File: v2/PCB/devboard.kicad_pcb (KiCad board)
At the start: 2 copper layers, 51 x 21 mm, 4 parts, among them J1 USB_C_Receptacle_USB2.0_14P, J2 Conn_01x20, J3 Conn_01x20, J4 Conn_01x03

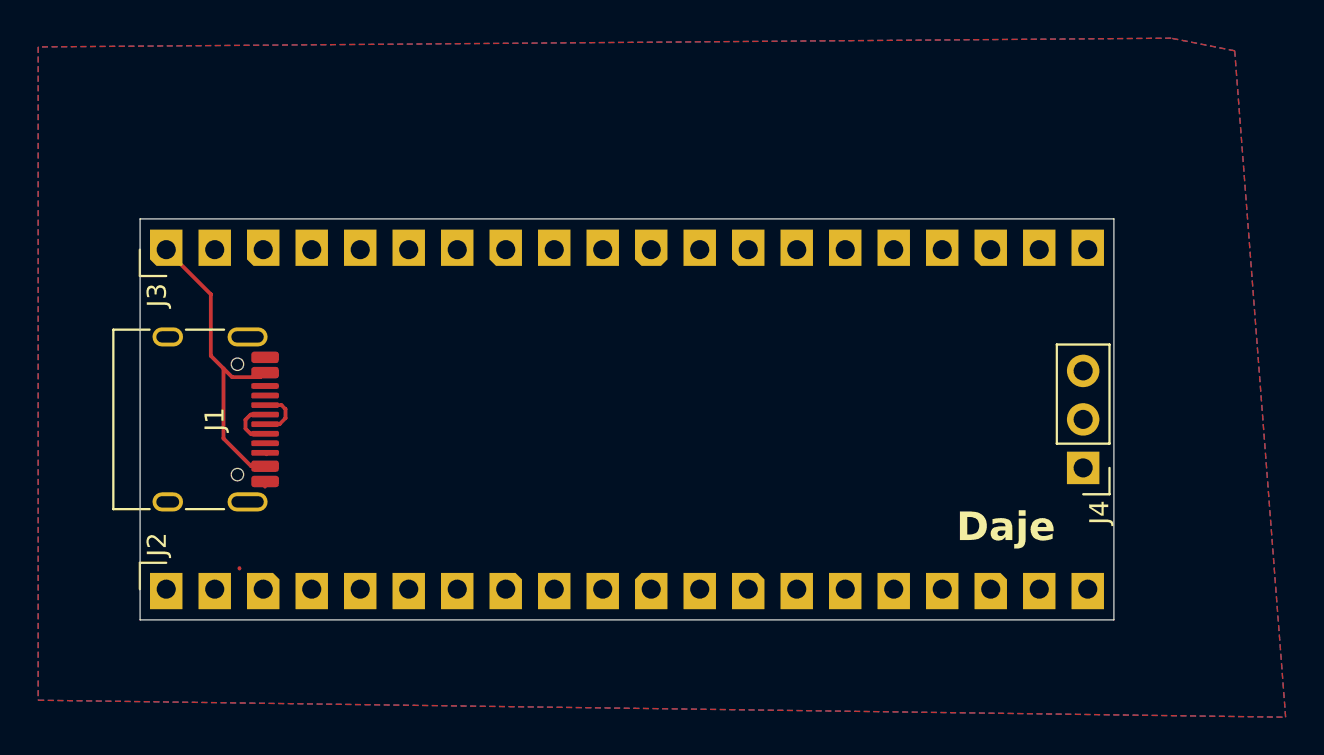
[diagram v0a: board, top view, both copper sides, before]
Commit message: added imu to the v2 and created/wired pcb
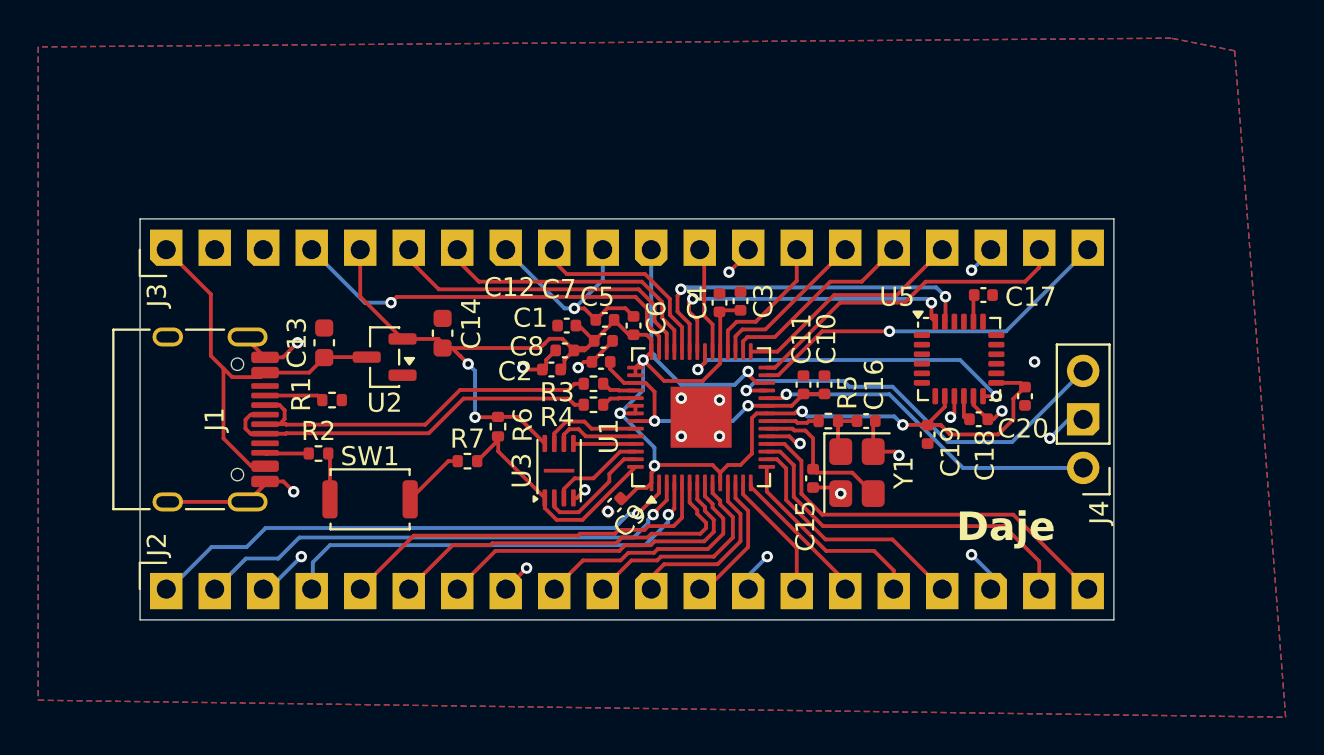
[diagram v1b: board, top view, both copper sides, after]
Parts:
- added C1: 1uF, Capacitor_SMD:C_0402_1005Metric, F.Cu at (111.5, 62.6)
- added C10: 0.1uF, Capacitor_SMD:C_0402_1005Metric, F.Cu at (125.0, 65.7)
- added C11: 0.1uF, Capacitor_SMD:C_0402_1005Metric, F.Cu at (123.9, 65.7)
- added C12: 1uF, Capacitor_SMD:C_0402_1005Metric, F.Cu at (113.3, 64.5)
- added C13: 10uF, Capacitor_SMD:C_0603_1608Metric, F.Cu at (98.8, 63.5)
- added C14: 10uF, Capacitor_SMD:C_0603_1608Metric, F.Cu at (105.0, 63.0)
- added C15: 33pF, Capacitor_SMD:C_0402_1005Metric, F.Cu at (124.4, 70.6)
- added C16: 33pF, Capacitor_SMD:C_0402_1005Metric, F.Cu at (127.2, 67.6)
- added C17: 2.2Nf, Capacitor_SMD:C_0402_1005Metric, F.Cu at (133.3, 61.0)
- added C18: 0.1uF, Capacitor_SMD:C_0402_1005Metric, F.Cu at (133.1, 67.5)
- added C19: 10nF, Capacitor_SMD:C_0402_1005Metric, F.Cu at (130.4, 68.3)
- added C2: 0.1uF, Capacitor_SMD:C_0402_1005Metric, F.Cu at (110.7, 64.9)
- added C20: 0.1uF, Capacitor_SMD:C_0402_1005Metric, F.Cu at (135.5, 66.3)
- added C3: 0.1uF, Capacitor_SMD:C_0402_1005Metric, F.Cu at (120.6, 61.3)
- added C4: 0.1uF, Capacitor_SMD:C_0402_1005Metric, F.Cu at (119.5, 61.4)
- added C5: 0.1uF, Capacitor_SMD:C_0402_1005Metric, F.Cu at (113.5, 62.3)
- added C6: 0.1uF, Capacitor_SMD:C_0402_1005Metric, F.Cu at (115.0, 62.6)
- added C7: 0.1uF, Capacitor_SMD:C_0402_1005Metric, F.Cu at (113.4, 63.4)
- added C8: 0.1uF, Capacitor_SMD:C_0402_1005Metric, F.Cu at (111.4, 63.9)
- added C9: 0.1uF, Capacitor_SMD:C_0402_1005Metric, F.Cu at (114.0, 72.0)
- added R1: 5.1K, Resistor_SMD:R_0402_1005Metric, F.Cu at (99.2, 66.5)
- added R2: 5.1K, Resistor_SMD:R_0402_1005Metric, F.Cu at (98.5, 69.3)
- added R3: 27, Resistor_SMD:R_0402_1005Metric, F.Cu at (112.9, 65.6)
- added R4: 27, Resistor_SMD:R_0402_1005Metric, F.Cu at (112.9, 66.7)
- added R5: 1K, Resistor_SMD:R_0402_1005Metric, F.Cu at (125.2, 67.6)
- added R6: 10K, Resistor_SMD:R_0402_1005Metric, F.Cu at (107.9, 67.9)
- added R7: 1K, Resistor_SMD:R_0402_1005Metric, F.Cu at (106.3, 69.7)
- added SW1: SW_Push, Button_Switch_SMD:SW_Push_SPST_NO_Alps_SKRK, F.Cu at (101.2, 71.7)
- added U1: RP2040, Package_DFN_QFN:QFN-56-1EP_7x7mm_P0.4mm_EP3.2x3.2mm, F.Cu at (118.5, 67.4)
- added U2: MCP1700x-330xxTT, Package_TO_SOT_SMD:SOT-23, F.Cu at (102.0, 64.2)
- added U3: W25Q16JVUXIQ TR, Package_SON:Winbond_USON-8-1EP_3x2mm_P0.5mm_EP0.2x1.6mm, F.Cu at (111.1, 70.2)
- added U5: MPU-6050, Sensor_Motion:InvenSense_QFN-24_4x4mm_P0.5mm, F.Cu at (132.1, 64.3)
- added Y1: Crystal_GND24, Crystal:Crystal_SMD_3225-4Pin_3.2x2.5mm, F.Cu at (126.7, 70.3)
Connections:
- J3 pad 10: GPIO23 -> GND
- J3 pad 2: GPIO29_ADC3 -> GND
- J3 pad 4: GPIO28_ADC2 -> GPIO29_ADC3
- J3 pad 6: GPIO27_ADC1 -> GPIO28_ADC2
- J3 pad 7: GPIO26_ADC0 -> GPIO27_ADC1
- J3 pad 9: GPIO24 -> GPIO26_ADC0
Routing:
- net +3.3V: track 0.00 -> 83.9 mm, vias 0 -> 7
- net GND: track 1.28 -> 56.4 mm, vias 0 -> 24
- net GPIO0: track 0.00 -> 28.4 mm, vias 0 -> 1
- net GPIO1: track 0.00 -> 28.1 mm, vias 0 -> 1
- net GPIO2: track 0.00 -> 23.1 mm, vias 0 -> 1
- net SWD: track 0.00 -> 21.8 mm, vias 0 -> 1
- net GPIO29_ADC3: track 0.00 -> 21.6 mm, vias 0 -> 1
- net GPIO15: track 0.00 -> 21.0 mm
- net GPIO3: track 0.00 -> 20.2 mm
- net GPIO4: track 0.00 -> 19.6 mm
- net GPIO16: track 0.00 -> 19.5 mm, vias 0 -> 1
- net GPIO14: track 0.00 -> 19.1 mm
- net SCL: track 0.00 -> 19.0 mm, vias 0 -> 2
- net SWCLK: track 0.00 -> 18.2 mm, vias 0 -> 1
- net GPIO23: track 0.36 -> 18.5 mm, vias 0 -> 2
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
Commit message: updated pcb and made renders
-Changed imu to a MPU-6500
-moved some traces and changed some pads in the devboard
-remade gerber and BOM
-created renders of the v2
-made pinout image of the v2
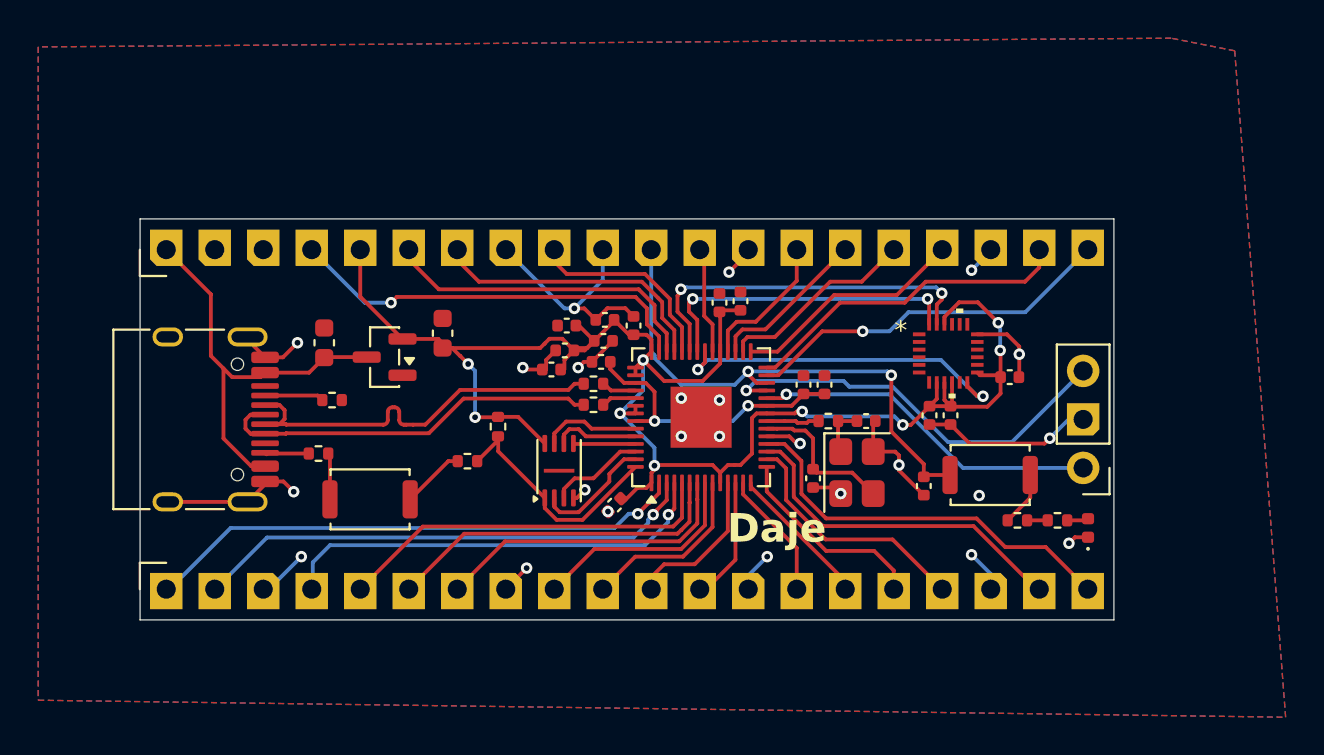
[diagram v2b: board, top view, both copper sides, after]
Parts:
- removed C17: 2.2Nf, Capacitor_SMD:C_0402_1005Metric
- removed C19: 10nF, Capacitor_SMD:C_0402_1005Metric
- added C21: 100nF, Capacitor_SMD:C_0402_1005Metric, F.Cu at (130.2, 71.0)
- added C22: 10nF, Capacitor_SMD:C_0402_1005Metric, F.Cu at (130.5, 67.3)
- added D2: LED, LED_SMD:LED_0402_1005Metric, F.Cu at (138.8, 73.2)
- added R8: 1K, Resistor_SMD:R_0402_1005Metric, F.Cu at (135.1, 72.8)
- added R9: 150, Resistor_SMD:R_0402_1005Metric, F.Cu at (137.2, 72.8)
- added SW2: SW_Push, Button_Switch_SMD:SW_Push_SPST_NO_Alps_SKRK, F.Cu at (133.7, 70.4)
- U5: value MPU-6050 -> MPU-6500; footprint Sensor_Motion:InvenSense_QFN-24_4x4mm_P0.5mm -> mpu 6500:QFN24_3X3X0P9_IVS
- moved C20 4.03 mm to (131.6, 67.3), turned to -90 degrees
- moved C18 2.74 mm to (134.7, 65.3)
- moved U5 0.64 mm to (131.5, 64.1)
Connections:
- C18 pad 1: Net-(U5-REGOUT) -> +3.3V
- C20 pad 1: GND -> +3.3V
- C20 pad 2: +3.3V -> GND
- U5 pad 1: GND -> unconnected-(U5-NC-Pad1)
- U5 pad 10: Net-(U5-REGOUT) -> +3.3V
- U5 pad 11: GND -> unconnected-(U5-FSYNC-Pad11)
- U5 pad 20: Net-(U5-CPOUT) -> unconnected-(U5-RESV-Pad20)
- U5 pad 22: unconnected-(U5-RESV-Pad22) -> +3.3V
- U5 pad 9: GND -> +3.3V
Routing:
- net RUN: track 12.9 -> 27.9 mm, vias 1 -> 2
- net GND: track 56.4 -> 67.4 mm
- net +3.3V: track 83.9 -> 90.6 mm, vias 7 -> 9
- net Net-(R8-Pad2): track 0.00 -> 2.87 mm
- net GPIO7: track 11.2 -> 9.41 mm
- net GPIO6: track 13.1 -> 11.5 mm
- net GPIO5: track 17.6 -> 16.1 mm
- net Net-(U5-CPOUT): track 1.42 -> 0.00 mm
- net GPIO4: track 19.6 -> 18.2 mm
- net USBC_D-: track 19.6 -> 21.0 mm
- net GPIO8: track 9.42 -> 8.16 mm
- net Net-(U5-REGOUT): track 1.25 -> 0.00 mm
- net Net-(D2-A): track 0.00 -> 1.15 mm
- net Net-(R8-Pad1): track 0.00 -> 1.08 mm
- net GPIO14: track 19.1 -> 18.2 mm
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
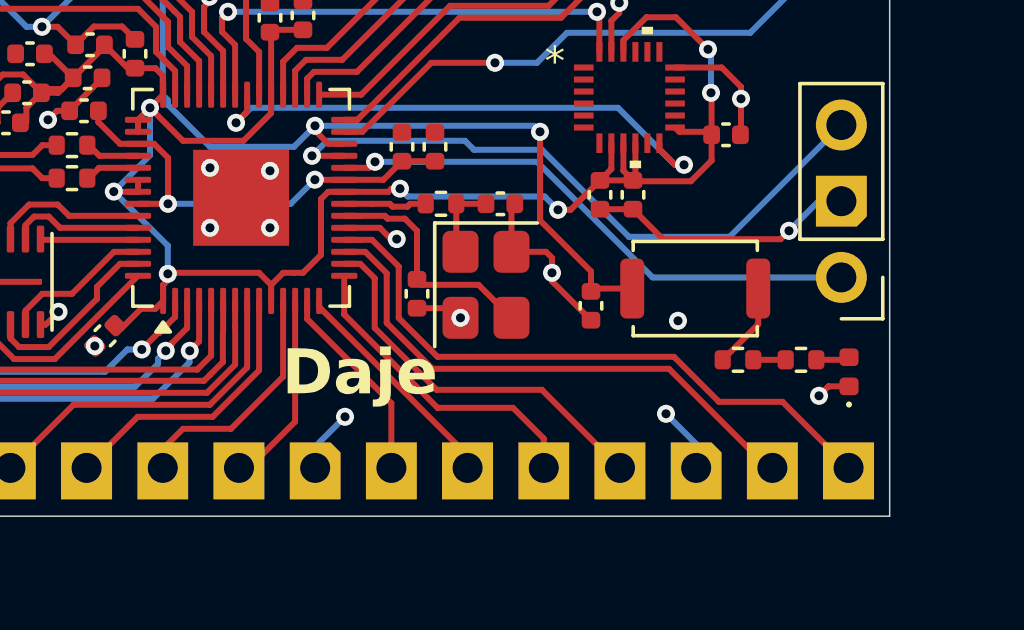
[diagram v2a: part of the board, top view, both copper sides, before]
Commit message: moved/updated files in the repo and updated readme
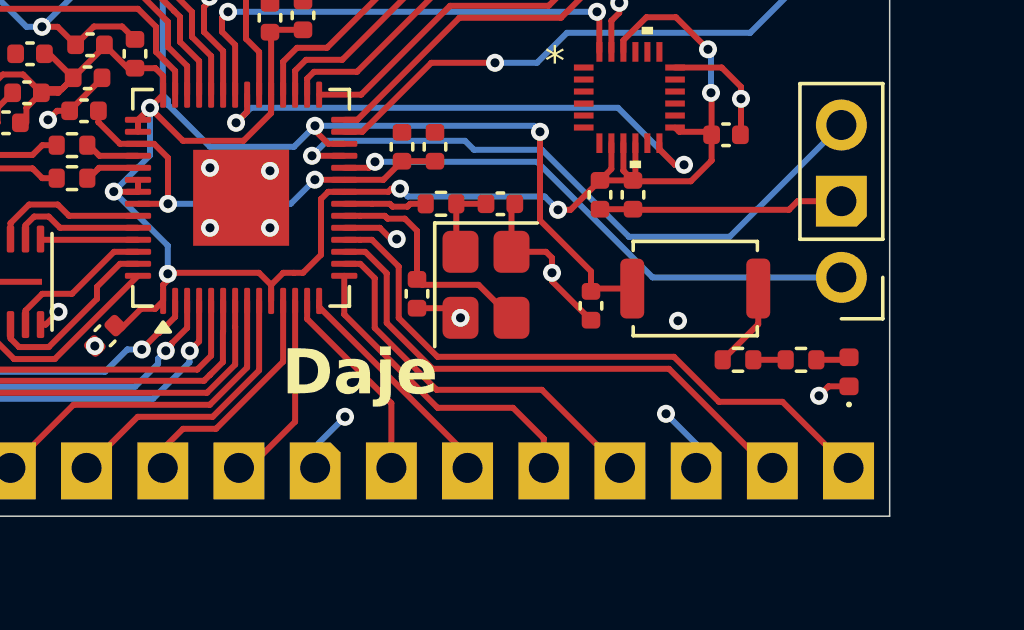
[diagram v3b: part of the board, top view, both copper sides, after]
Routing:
- net GND: track 67.4 -> 67.3 mm, vias 24 -> 23
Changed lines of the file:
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@@
-	)
-	(segment
-		(start 136.52 68.78)
-		(end 136.8 68.5)
-		(width 0.2)
-		(layer "F.Cu")
-		(net "GND")
 	)
 	(segment
@@
 	)
 	(segment
-		(start 131.6 67.78)
-		(end 132.6 68.78)
-		(width 0.2)
-		(layer "F.Cu")
-		(net "GND")
-	)
-	(segment
 		(start 94.7856 71.8332)
 		(end 90.6056 71.8332)
@@
 	)
 	(segment
+		(start 137.0868 67.5132)
+		(end 138.5456 67.5132)
+		(width 0.2)
+		(layer "F.Cu")
+		(net "GND")
+	)
+	(segment
 		(start 110.42 64.9)
 		(end 109.3 64.9)
@@
 	)
 	(segment
+		(start 136.8 67.8)
+		(end 137.0868 67.5132)
+		(width 0.2)
+		(layer "F.Cu")
+		(net "GND")
+	)
+	(segment
 		(start 121.975 68.4)
 		(end 123.158241 68.4)
@@
 	)
 	(segment
+		(start 131.62 67.8)
+		(end 131.6 67.78)
+		(width 0.2)
+		(layer "F.Cu")
+		(net "GND")
+	)
+	(segment
 		(start 130.2 71.48)
 		(end 128.9 70.18)
@@
 	)
 	(segment
+		(start 136.8 67.8)
+		(end 131.62 67.8)
+		(width 0.2)
+		(layer "F.Cu")
+		(net "GND")
+	)
+	(segment
 		(start 95.7006 70.9182)
 		(end 94.7856 71.8332)
@@
 	)
 	(segment
-		(start 132.6 68.78)
-		(end 136.52 68.78)
-		(width 0.2)
-		(layer "F.Cu")
-		(net "GND")
-	)
-	(segment
 		(start 112.4 64.5)
 		(end 112.1 64.8)
@@
 	)
 	(via
-		(at 136.8 68.5)
-		(size 0.6)
-		(drill 0.3)
-		(layers "F.Cu" "B.Cu")
-		(net "GND")
-	)
-	(via
 		(at 120 59.8)
 		(size 0.6)
@@
 	)
 	(segment
-		(start 138.5456 67.5132)
-		(end 137.7868 67.5132)
-		(width 0.2)
-		(layer "B.Cu")
-		(net "GND")
-	)
-	(segment
 		(start 133.7056 76.4032)
 		(end 133.7056 75.6056)
@@
 	)
 	(segment
-		(start 137.7868 67.5132)
-		(end 136.8 68.5)
-		(width 0.2)
-		(layer "B.Cu")
-		(net "GND")
-	)
-	(segment
 		(start 111.3824 61.7)
 		(end 111.9 61.7)
@@
 	)
 	(segment
+		(start 137.7868 67.5132)
+		(end 138.5456 67.5132)
+		(width 0.2)
+		(layer "B.Cu")
+		(net "GND")
+	)
+	(segment
 		(start 94.94319 68.2632)
 		(end 95.7006 68.2632)
@@
 	)
 	(segment
-		(start 119.9375 70.8375)
-		(end 119.9375 73.3625)
-		(width 0.2)
-		(layer "F.Cu")
-		(net "GPIO8")
-	)
-	(segment
-		(start 119.9375 73.3625)
-		(end 118.2 75.1)
-		(width 0.2)
-		(layer "F.Cu")
-		(net "GPIO8")
-	)
-	(segment
 		(start 116.6 75.1)
 		(end 115.9256 75.7744)
@@
 	)
 	(segment
-		(start 118.2 75.1)
+		(start 117.7 75.1)
 		(end 116.6 75.1)
 		(width 0.2)
 		(layer "F.Cu")
+		(net "GPIO8")
+	)
+	(segment
+		(start 119.9375 72.8625)
+		(end 117.7 75.1)
+		(width 0.2)
+		(layer "F.Cu")
+		(net "GPIO8")
+	)
+	(segment
+		(start 119.9375 70.8375)
+		(end 119.9375 72.8625)
+		(width 0.2)
+		(layer "F.Cu")
